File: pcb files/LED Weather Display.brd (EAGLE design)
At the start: 69.8 x 36.8 mm, 8 parts, among them IC1 74HCT245N, J1 POWER_JACK

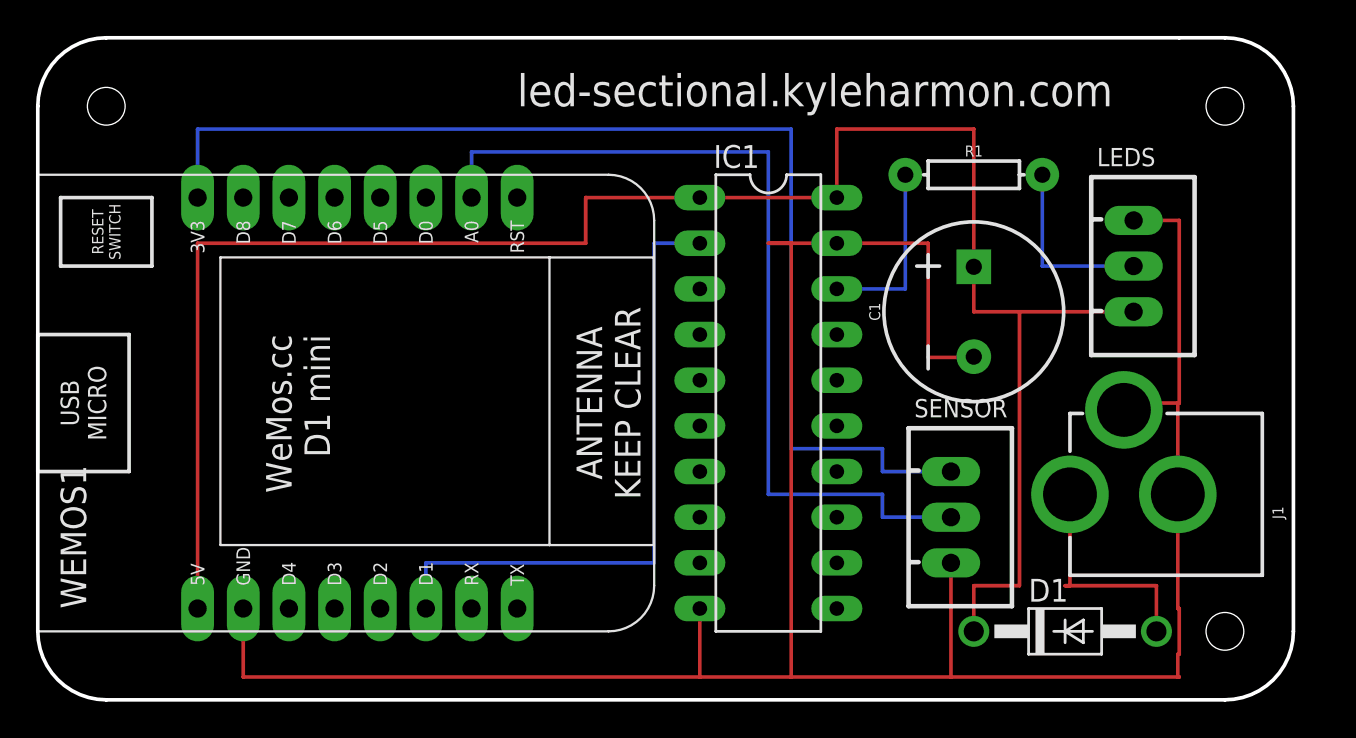
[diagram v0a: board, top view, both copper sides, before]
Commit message: Update for digital light sensor.
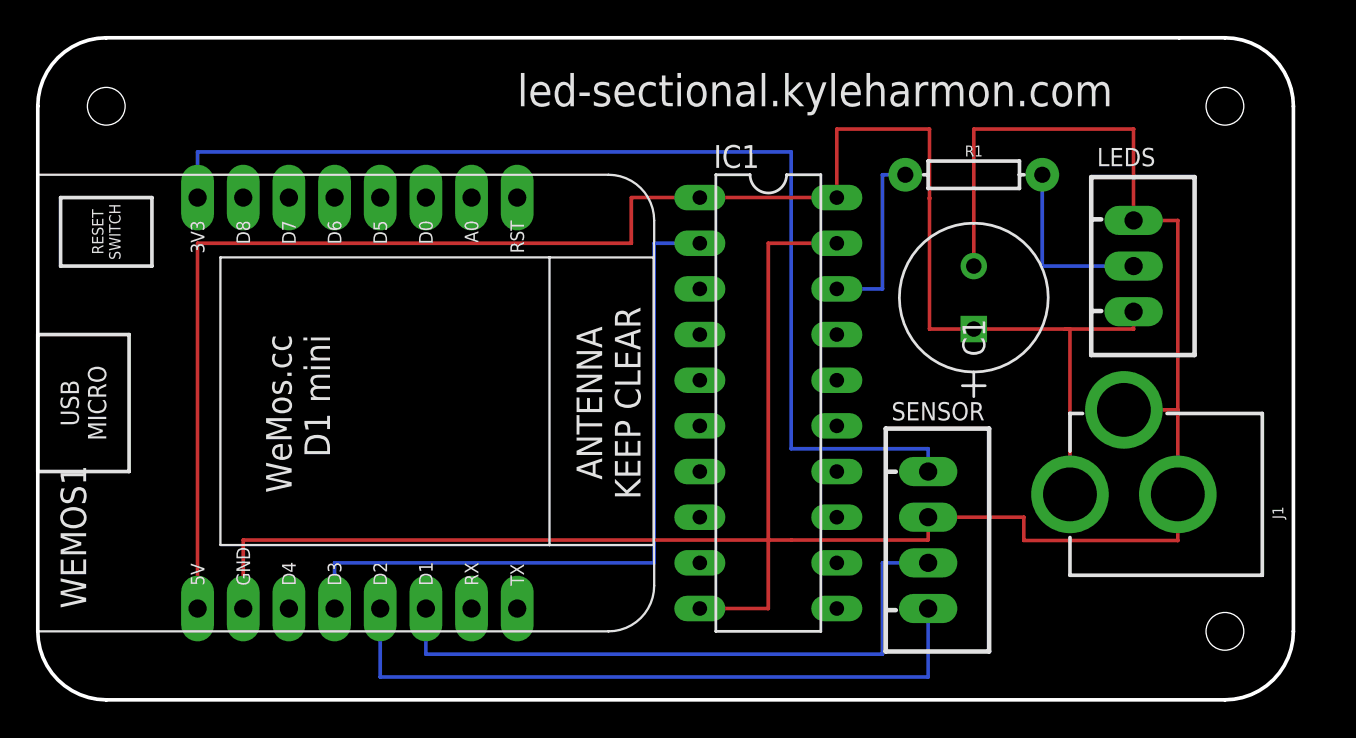
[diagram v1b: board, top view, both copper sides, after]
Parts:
- removed D1: 1N4004, diode:DO41-10
- C1: value 1mF -> RL80J102MDN1KX; device SparkFun-Capacitors:CPOL-RADIAL-5MM-10MM -> Kyle's Custom:RL8
- SENSOR: value JST-XH-03-PIN-LONG-PAD -> JST-XH-04-PIN-LONG-PAD; device Rembrandt Electronics - JST XH Connectors v1-0:JST-XH-03-PACKAGE-LONG-PAD -> Rembrandt Electronics - JST XH Connectors v1-0:JST-XH-04-PACKAGE-LONG-PAD
- moved C1 2.54 mm to (52.1, 24.1)
- moved SENSOR 1.80 mm to (49.5, 8.89)
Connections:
- removed net N$1 (its old number): SENSOR.2, WEMOS1.A0
- new net N$5: SENSOR.3, WEMOS1.D1
- net GND: now also C1.2, SENSOR.2; no longer C1.-, SENSOR.3
- net N$3: now also WEMOS1.D3; no longer WEMOS1.D1
- net N$6: now also SENSOR.4, WEMOS1.D2; no longer D1.A, J1.PWR
- net VCC: now also C1.1, J1.PWR; no longer C1.+, D1.C
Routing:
- net N$1 (its old number): track 49.5 -> 0.00 mm
- net N$5: track 0.00 -> 35.6 mm
- net N$6: track 13.0 -> 38.1 mm
- net GND: track 141.0 -> 131.2 mm
- net VCC: track 109.2 -> 100.4 mm
- net N$1: track 67.3 -> 61.0 mm
- net N$3: track 35.6 -> 40.6 mm

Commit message: Update board layouts and kit information in documentation.
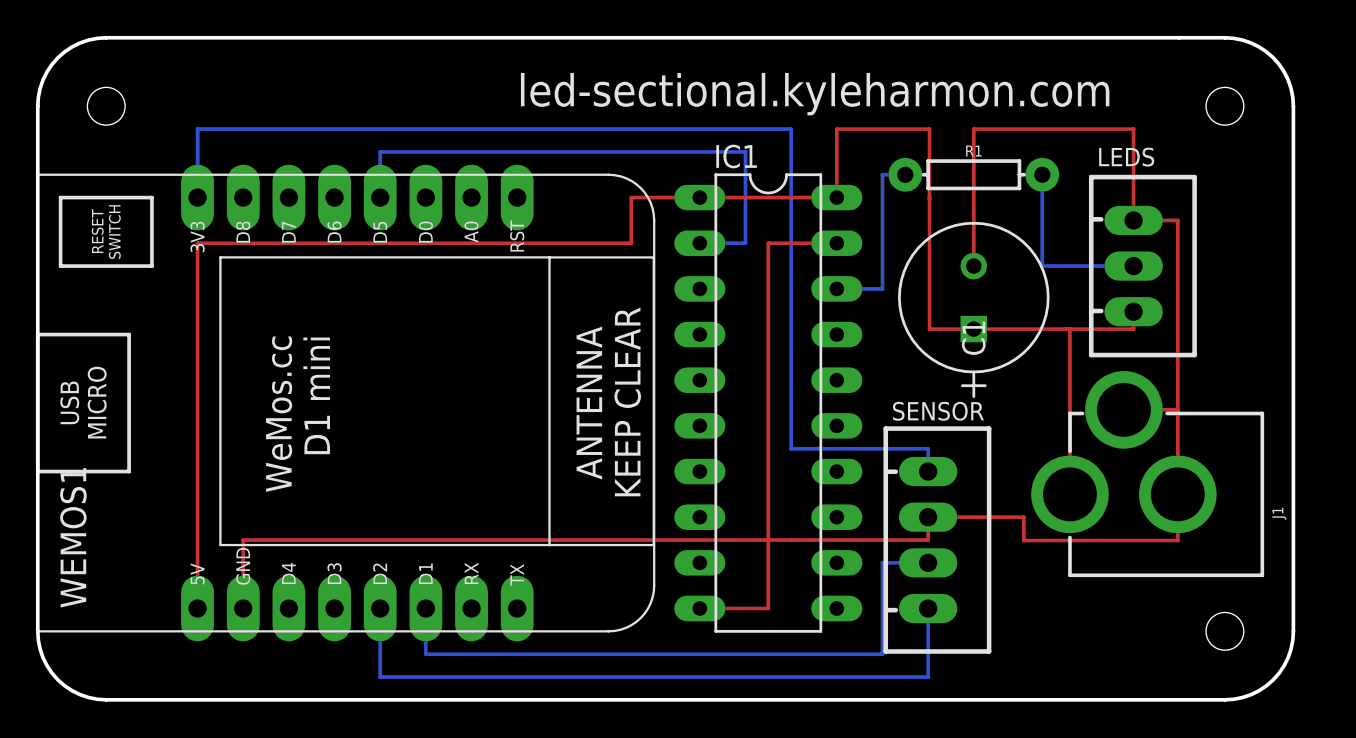
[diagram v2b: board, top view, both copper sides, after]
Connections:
- net N$3: now also WEMOS1.D5; no longer WEMOS1.D3
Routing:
- net N$3: track 40.6 -> 30.5 mm
- net N$1: track 61.0 -> 63.5 mm
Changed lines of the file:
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@@
 <wire x1="57.42" y1="20.6248" x2="57.15" y2="20.6248" width="0.2032" layer="1"/>
-</signal>
-<signal name="N$3">
-<contactref element="IC1" pad="2"/>
-<contactref element="WEMOS1" pad="D3"/>
-<wire x1="16.51" y1="5.08" x2="16.51" y2="7.62" width="0.2032" layer="16"/>
-<wire x1="16.51" y1="7.62" x2="34.29" y2="7.62" width="0.2032" layer="16"/>
-<wire x1="34.29" y1="7.62" x2="34.29" y2="25.4" width="0.2032" layer="16"/>
-<wire x1="34.29" y1="25.4" x2="36.83" y2="25.4" width="0.2032" layer="16"/>
 </signal>
 <signal name="N$4">
@@
 <contactref element="WEMOS1" pad="3V3"/>
 <contactref element="SENSOR" pad="1"/>
-<wire x1="8.89" y1="27.94" x2="8.89" y2="30.48" width="0.2032" layer="16"/>
-<wire x1="8.89" y1="30.48" x2="41.91" y2="30.48" width="0.2032" layer="16"/>
-<wire x1="41.91" y1="30.48" x2="41.91" y2="13.97" width="0.2032" layer="16"/>
 <wire x1="41.91" y1="13.97" x2="49.53" y2="13.97" width="0.2032" layer="16"/>
 <wire x1="49.53" y1="13.97" x2="49.53" y2="12.7" width="0.2032" layer="16"/>
+<wire x1="8.89" y1="31.75" x2="41.91" y2="31.75" width="0.2032" layer="16"/>
+<wire x1="8.89" y1="27.94" x2="8.89" y2="31.75" width="0.2032" layer="16"/>
+<wire x1="41.91" y1="31.75" x2="41.91" y2="13.97" width="0.2032" layer="16"/>
 </signal>
 <signal name="N$5">
@@
 <wire x1="49.53" y1="1.27" x2="49.53" y2="5.08" width="0.2032" layer="16"/>
 </signal>
+<signal name="N$3">
+<contactref element="WEMOS1" pad="D5"/>
+<contactref element="IC1" pad="2"/>
+<wire x1="19.05" y1="27.94" x2="19.05" y2="30.48" width="0.2032" layer="16"/>
+<wire x1="19.05" y1="30.48" x2="39.37" y2="30.48" width="0.2032" layer="16"/>
+<wire x1="39.37" y1="30.48" x2="39.37" y2="25.4" width="0.2032" layer="16"/>
+<wire x1="39.37" y1="25.4" x2="36.83" y2="25.4" width="0.2032" layer="16"/>
+</signal>
 </signals>
